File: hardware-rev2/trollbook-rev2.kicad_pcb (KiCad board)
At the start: 4 copper layers, 100 x 100 mm, 9 parts, among them U1 MC68040FC33V, U2 EPF10K50VRC240, U3 EPC2, U4 HY57V561620, U5 HY57V561620, U6 AS7C34098, U7 74LVC138, U8 MCP4902, U9 S25FL204K0TMFI010

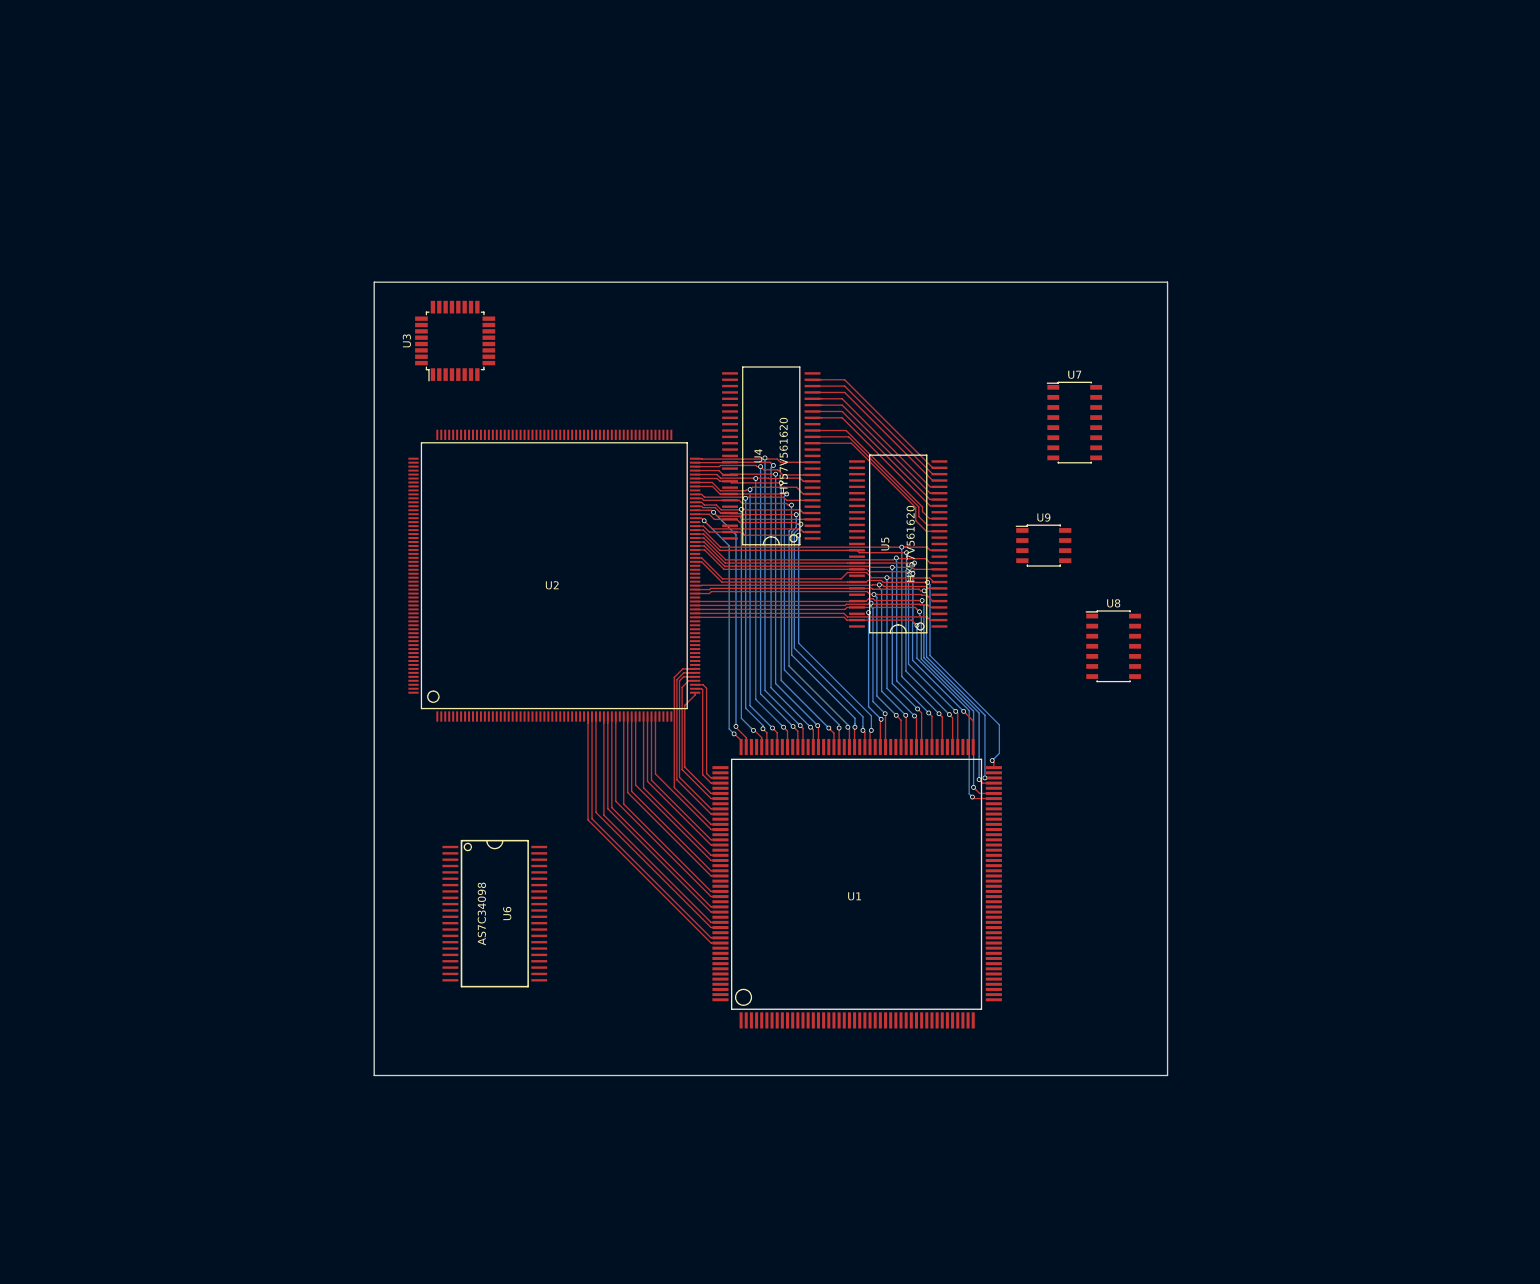
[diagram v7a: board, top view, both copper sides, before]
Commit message: cpu control signals, vga dac
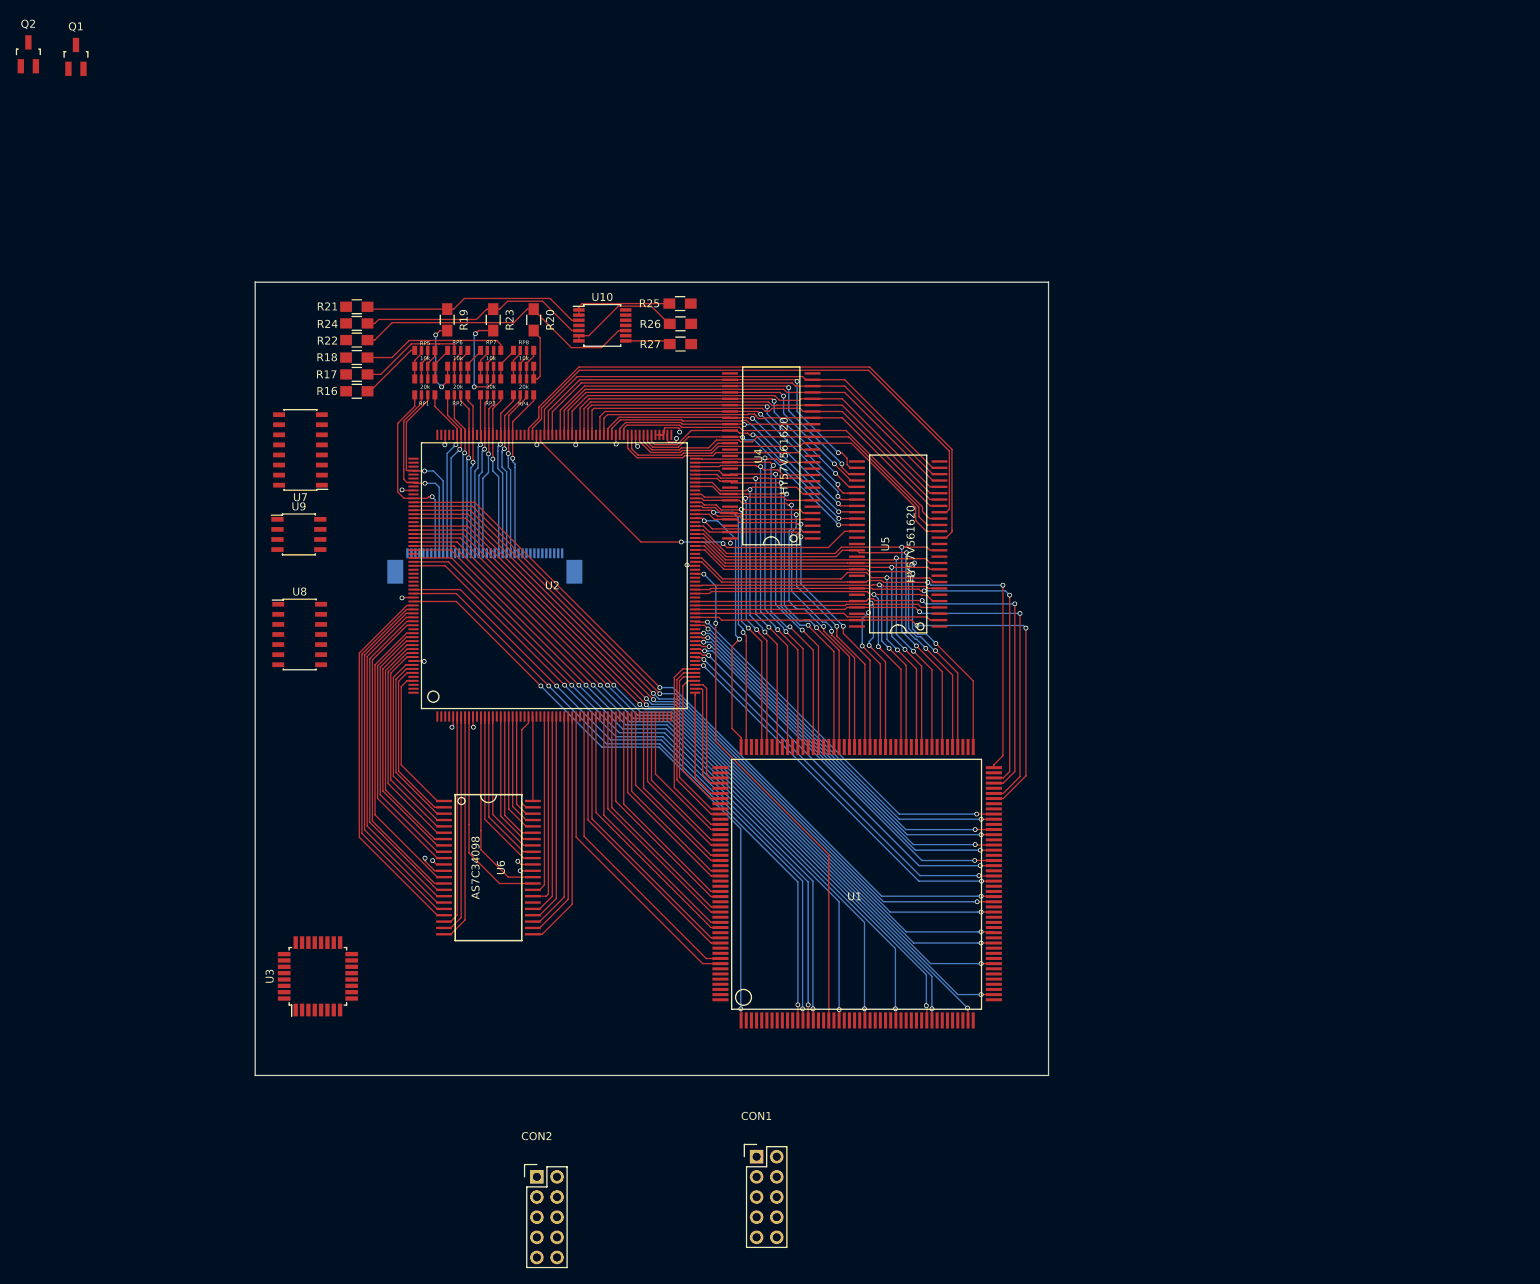
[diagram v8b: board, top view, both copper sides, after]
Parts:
- added CON1: FPGA JTAG, Pin_Headers:Pin_Header_Straight_2x05, F.Cu at (148.2, 160.2)
- added CON2: CPU JTAG, Pin_Headers:Pin_Header_Straight_2x05, F.Cu at (120.5, 162.8)
- added P4: ER-CON40HT-1, mod:ER-CON40HT-1, B.Cu at (123.7, 84.2)
- added Q1: 2N7002E, Housings_SOT-23_SOT-143_TSOT-6:SOT-23_Handsoldering, F.Cu at (62.4, 21.6)
- added Q2: 2N7002E, Housings_SOT-23_SOT-143_TSOT-6:SOT-23_Handsoldering, F.Cu at (56.4, 21.3)
- added R16: 10k, Resistors_SMD:R_0805_HandSoldering, F.Cu at (97.8, 63.8)
- added R17: 10k, Resistors_SMD:R_0805_HandSoldering, F.Cu at (97.8, 61.6)
- added R18: 10k, Resistors_SMD:R_0805_HandSoldering, F.Cu at (97.8, 59.5)
- added R19: 560k, Resistors_SMD:R_0805_HandSoldering, F.Cu at (109.2, 54.8)
- added R20: 560k, Resistors_SMD:R_0805_HandSoldering, F.Cu at (120.1, 54.8)
- added R21: 180k, Resistors_SMD:R_0805_HandSoldering, F.Cu at (97.8, 53.1)
- added R22: 180k, Resistors_SMD:R_0805_HandSoldering, F.Cu at (97.8, 57.3)
- added R23: 560k, Resistors_SMD:R_0805_HandSoldering, F.Cu at (115.0, 54.8)
- added R24: 180k, Resistors_SMD:R_0805_HandSoldering, F.Cu at (97.8, 55.2)
- added R25: 75, Resistors_SMD:R_0805_HandSoldering, F.Cu at (138.6, 52.7)
- added R26: 75, Resistors_SMD:R_0805_HandSoldering, F.Cu at (138.6, 55.2)
- added R27: 75, Resistors_SMD:R_0805_HandSoldering, F.Cu at (138.6, 57.8)
- added RP1: 20k, mod:RPACK8_SMD, F.Cu at (106.3, 63.2)
- added RP2: 20k, mod:RPACK8_SMD, F.Cu at (110.5, 63.2)
- added RP3: 20k, mod:RPACK8_SMD, F.Cu at (114.6, 63.2)
- added RP4: 20k, mod:RPACK8_SMD, F.Cu at (118.8, 63.2)
- added RP5: 10k, mod:RPACK8_SMD, F.Cu at (106.3, 59.6)
- added RP6: 10k, mod:RPACK8_SMD, F.Cu at (110.5, 59.6)
- added RP7: 10k, mod:RPACK8_SMD, F.Cu at (114.6, 59.6)
- added RP8: 10k, mod:RPACK8_SMD, F.Cu at (118.8, 59.6)
- added U10: ADA4851-4, Housings_SSOP:TSSOP-14_4.4x5mm_Pitch0.65mm, F.Cu at (128.8, 55.5)
- moved U8 102.6 mm to (90.6, 94.4)
- moved U7 97.7 mm to (90.7, 71.1), turned to 180 degrees
- moved U9 93.9 mm to (90.5, 81.8)
- moved U3 81.9 mm to (92.9, 137.5)
- moved U6 5.85 mm to (114.4, 123.8)
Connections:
- U1 pad 1: (no net) -> /CPURSTO
- U1 pad 12: (no net) -> /CPURSTI
- U1 pad 13: (no net) -> /CPUIPL2
- U1 pad 14: (no net) -> /CPUIPL1
- U1 pad 15: (no net) -> /CPUIPL0
- U1 pad 176: (no net) -> /CPUTT1
- U1 pad 177: (no net) -> /CPUTT0
- U1 pad 18: (no net) -> /CLK33
- U1 pad 20: (no net) -> /CPULFO
- U1 pad 25: (no net) -> /CPUSCD
- U1 pad 31: (no net) -> /CPUTBI
- U1 pad 37: (no net) -> /CPUTEA
- U1 pad 38: (no net) -> /CPUTA
- U1 pad 45: (no net) -> /CPUTIP
- U1 pad 48: (no net) -> /CPUTP
- U1 pad 54: (no net) -> /CPUSIZ1
- U1 pad 58: (no net) -> /CPURW
- U1 pad 60: (no net) -> /CPUSIZ0
- U1 pad 64: (no net) -> /CPUTM0
- U1 pad 66: (no net) -> /CPUTM1
- U1 pad 67: (no net) -> /CPUTM2
- U2 pad 11: (no net) -> /SPI1CLK
- U2 pad 12: /LLA5 -> /LLD11
- U2 pad 128: /RAM0UDQM -> /RAMCAS
- U2 pad 129: /RAM0LDQM -> /RAM0UDQM
- U2 pad 13: /LLA6 -> /LLD12
- U2 pad 132: /RAM0CS -> /RAM0LDQM
- U2 pad 134: /RAMCAS -> /RAMA12
- U2 pad 136: /RAMB1 -> /RAM0CS
- U2 pad 137: /RAMB0 -> /RAMA11
- U2 pad 138: /RAMA12 -> /RAMB0
- U2 pad 139: /RAMA11 -> /RAMA9
- U2 pad 14: /LLA7 -> /LLD13
- U2 pad 141: /RAMA10 -> /RAMB1
- U2 pad 142: /RAMA9 -> /RAMA8
- U2 pad 143: /RAMA8 -> /RAMA10
- U2 pad 146: /RAMA6 -> /RAMA0
- U2 pad 147: /RAMA5 -> /RAMA6
- U2 pad 148: /RAMA4 -> /RAMA1
- U2 pad 149: /RAMA3 -> /RAMA5
- U2 pad 15: /LLA8 -> /LLD14
- U2 pad 152: /RAMA1 -> /RAMA4
- U2 pad 153: /RAMA0 -> /RAMA3
- U2 pad 156: /RAM1LDQM -> /RAM1CS
- U2 pad 157: /RAM1CS -> /RAM1LDQM
- U2 pad 158: (no net) -> /VGAVSYNC
- U2 pad 159: (no net) -> /VGAHSYNC
- U2 pad 161: (no net) -> /VGAB4
- U2 pad 162: (no net) -> /VGAB3
- U2 pad 163: (no net) -> /VGAB2
- U2 pad 164: (no net) -> /VGAB1
- U2 pad 166: (no net) -> /VGAB0
- U2 pad 167: (no net) -> /VGAG5
- U2 pad 168: (no net) -> /VGAG4
- U2 pad 169: (no net) -> /VGAG3
- U2 pad 17: /LLA9 -> /LLD15
- U2 pad 171: (no net) -> /VGAG2
- U2 pad 172: (no net) -> /VGAG1
- U2 pad 173: (no net) -> /VGAG0
- U2 pad 174: (no net) -> /VGAR4
- U2 pad 175: (no net) -> /VGAR3
- U2 pad 18: /LLA10 -> /LLLB
- U2 pad 182: (no net) -> /SPI0SSBIT2
- U2 pad 183: (no net) -> /SPI0SSBIT1
- U2 pad 184: (no net) -> /VGAR2
- U2 pad 185: (no net) -> /SPI0SSBIT0
- U2 pad 186: (no net) -> /SPI0MISO
- U2 pad 187: (no net) -> /VGAR1
- U2 pad 188: (no net) -> /SPI0MOSI
- U2 pad 19: /LLA11 -> /LLUB
- U2 pad 190: (no net) -> /SPI0CLK
- U2 pad 191: (no net) -> /VGAR0
- U2 pad 192: (no net) -> /CPUTM2
- U2 pad 193: (no net) -> /CPUTM1
- U2 pad 194: (no net) -> /CPUTM0
- U2 pad 195: (no net) -> /CPUSIZ0
- U2 pad 196: (no net) -> /CPURW
- U2 pad 198: (no net) -> /CPUSIZ1
- U2 pad 199: (no net) -> /CPUTP
- U2 pad 20: /LLA12 -> /LLOE
- U2 pad 200: (no net) -> /CPUTIP
- U2 pad 201: (no net) -> /CPUTA
- U2 pad 202: (no net) -> /CPUTEA
- U2 pad 203: (no net) -> /CPUTBI
- U2 pad 204: (no net) -> /CPUSCD
- U2 pad 206: (no net) -> /CPULFO
- U2 pad 207: (no net) -> /CPUIPL0
- U2 pad 208: (no net) -> /CPUIPL1
- U2 pad 21: /LLA13 -> /LLA16
- U2 pad 213: (no net) -> /SNDSYNC
- U2 pad 214: (no net) -> /CPUIPL2
- U2 pad 215: (no net) -> /CPURSTI
- U2 pad 217: (no net) -> /CPURSTO
- U2 pad 218: (no net) -> /LLA7
- U2 pad 219: /LLD15 -> /LLA6
- U2 pad 220: /LLD14 -> /LLWE
- U2 pad 221: /LLD13 -> /LLD7
- U2 pad 222: /LLD12 -> /LLD6
- U2 pad 223: /LLD11 -> /LLD5
- U2 pad 225: /LLD10 -> /LLD4
- U2 pad 226: /LLD9 -> /LLD3
- U2 pad 227: /LLD8 -> /LLD2
- U2 pad 228: /LLD7 -> /LLD1
- U2 pad 229: /LLD6 -> /LLD0
- U2 pad 230: /LLD5 -> /LLCE
- U2 pad 231: /LLD4 -> /LLA5
- U2 pad 233: /LLD3 -> /LLA4
- U2 pad 234: /LLD2 -> /LLA3
- U2 pad 235: /LLD1 -> /LLA2
- U2 pad 236: (no net) -> /SPI1SS
- U2 pad 237: /LLD0 -> /LLA1
- U2 pad 238: (no net) -> /SPI1MOSI
- U2 pad 24: /LLA14 -> /LLA17
- U2 pad 25: /LLA15 -> /LLA18
- U2 pad 28: /LLA16 -> /LLD9
- U2 pad 29: /LLA17 -> /LLD8
- U2 pad 30: /LLA18 -> /LLA15
- U2 pad 31: /LLCE -> /LLA14
- U2 pad 33: /LLWE -> /LLA13
- U2 pad 34: /LLLB -> /LLA12
- U2 pad 35: /LLUB -> /LLA11
- U2 pad 36: /LLOE -> /CPUTT0
- U2 pad 38: (no net) -> /CPUTT1
- U2 pad 6: /LLA1 -> /LLA8
- U2 pad 68: /A9 -> /A0
- U2 pad 7: /LLA2 -> /LLA9
- U2 pad 70: /A8 -> /A1
- U2 pad 71: /A7 -> /A2
- U2 pad 72: /A6 -> /A3
- U2 pad 73: /A5 -> /A4
- U2 pad 74: /A4 -> /A5
- U2 pad 75: /A3 -> /A6
- U2 pad 76: /A2 -> /A7
- U2 pad 78: /A1 -> /A8
- U2 pad 79: /A0 -> /A9
- U2 pad 8: /LLA3 -> /LLA10
- U2 pad 9: /LLA4 -> /LLD10
- U2 pad 91: (no net) -> /CLK33
- U7 pad 1: (no net) -> /SPI0SSBIT0
- U7 pad 14: (no net) -> /SPI0SS1
- U7 pad 2: (no net) -> /SPI0SSBIT1
- U7 pad 3: (no net) -> /SPI0SSBIT2
- U8 pad 1: (no net) -> +3V3
- U8 pad 11: (no net) -> +3V3
- U8 pad 12: (no net) -> GND
- U8 pad 13: (no net) -> +3V3
- U8 pad 3: (no net) -> /SPI1SS
- U8 pad 4: (no net) -> /SPI1CLK
- U8 pad 5: (no net) -> /SPI1MOSI
- U8 pad 8: (no net) -> /SNDSYNC
- U8 pad 9: (no net) -> +3V3
- U9 pad 1: (no net) -> /SPI0SS1
- U9 pad 2: (no net) -> /SPI0MISO
- U9 pad 3: (no net) -> +3V3
- U9 pad 4: (no net) -> GND
- U9 pad 5: (no net) -> /SPI0MOSI
- U9 pad 6: (no net) -> /SPI0CLK
- U9 pad 7: (no net) -> +3V3
- U9 pad 8: (no net) -> +3V3
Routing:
- net /CPUTP: track 0.00 -> 97.4 mm, vias 0 -> 2
- net /CPUTIP: track 0.00 -> 96.2 mm, vias 0 -> 2
- net /CPUSIZ1: track 0.00 -> 96.0 mm, vias 0 -> 2
- net /CPURW: track 0.00 -> 95.3 mm, vias 0 -> 2
- net /CPUSIZ0: track 0.00 -> 95.0 mm, vias 0 -> 2
- net /CPUTM0: track 0.00 -> 94.1 mm, vias 0 -> 2
- net /CPUTM1: track 0.00 -> 93.8 mm, vias 0 -> 2
- net /CPUTA: track 0.00 -> 93.8 mm, vias 0 -> 2
- net /CPUTM2: track 0.00 -> 93.7 mm, vias 0 -> 2
- net /CPUTEA: track 0.00 -> 93.0 mm, vias 0 -> 2
- net /CPUTBI: track 0.00 -> 90.8 mm, vias 0 -> 2
- net /CPUSCD: track 0.00 -> 88.7 mm, vias 0 -> 2
- net /CPULFO: track 0.00 -> 86.6 mm, vias 0 -> 2
- net /CPUIPL0: track 0.00 -> 84.6 mm, vias 0 -> 2
- net /CPUIPL1: track 0.00 -> 83.7 mm, vias 0 -> 2
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- added copper zone on In2.Cu, net +3V3
- added copper zone on In1.Cu, net GND
